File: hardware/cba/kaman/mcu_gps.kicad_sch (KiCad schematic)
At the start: 12 parts, among them Q1 MMDT5551, SW1 SW_Push, SW2 SW_Push, U1 ESP32-C6-WROOM-1-N8

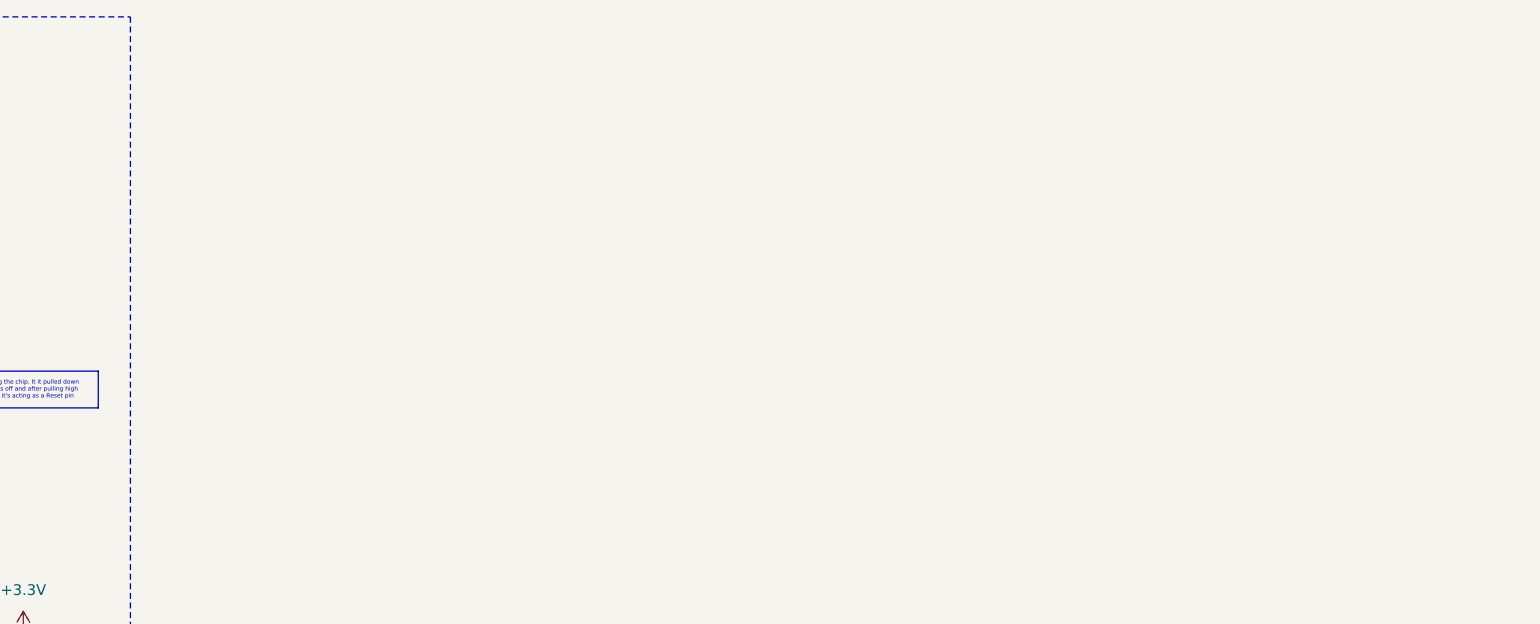
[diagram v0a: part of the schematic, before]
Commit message: hw(schmatic): add L80 GPS Module
L80 and the circuit such as the decoupling caps,reset and PPS pin, and
most importantly the backup battery (although the footprint has to be
checked)
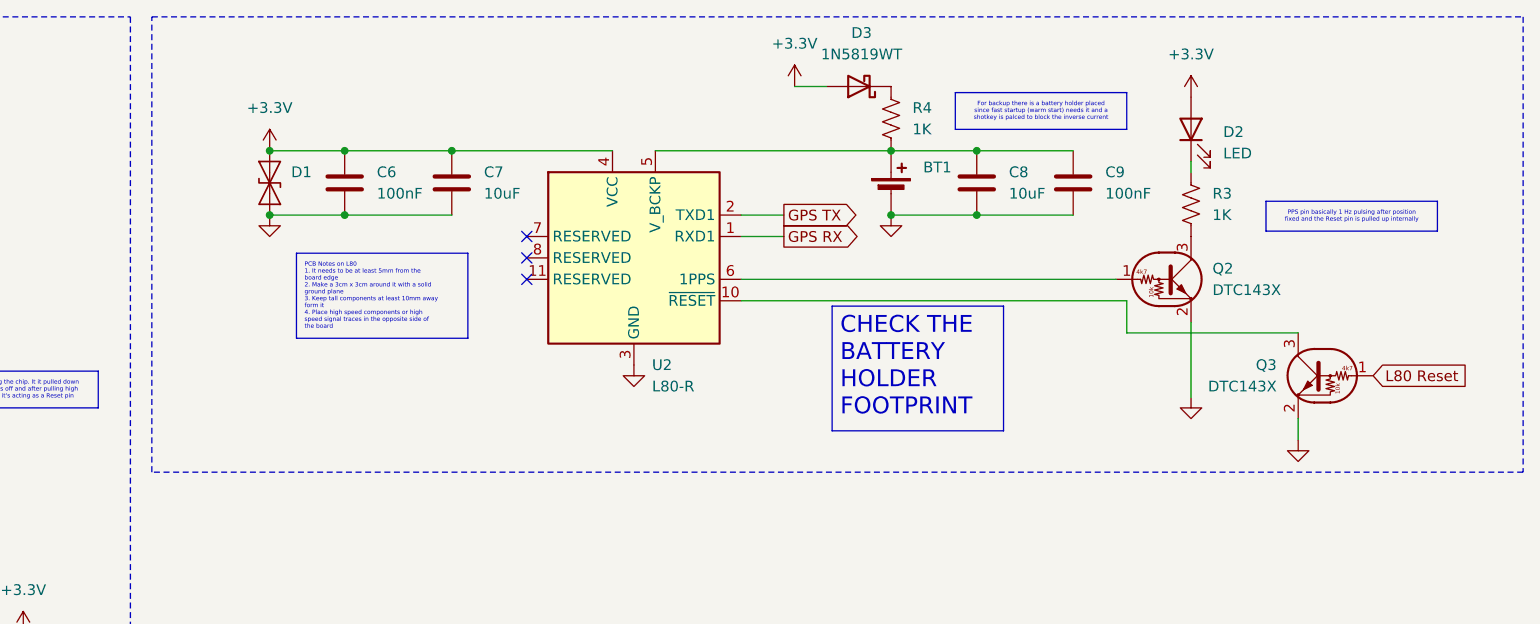
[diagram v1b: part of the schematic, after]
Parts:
- added BT1: Battery_Cell, Battery:BatteryHolder_Keystone_1060_1x2032, symbol Device:Battery_Cell
- added C6, C9: 100nF, Capacitor_SMD:C_0603_1608Metric_Pad1.08x0.95mm_HandSolder, symbol Device:C
- added C7, C8: 10uF, Capacitor_SMD:C_0805_2012Metric_Pad1.18x1.45mm_HandSolder, symbol Device:C
- added D1: SD03C-MMD, Diode_SMD:D_SOD-323_HandSoldering, symbol Diode:SD05C-01F
- added D2: LED, LED_SMD:LED_0603_1608Metric_Pad1.05x0.95mm_HandSolder, symbol Device:LED
- added D3: 1N5819WT, Diode_SMD:D_SOD-523, symbol Diode:1N5819WS
- added Q2, Q3: DTC143X, symbol Transistor_BJT:DTC143X
- added R3, R4: 1K, Resistor_SMD:R_0603_1608Metric_Pad0.98x0.95mm_HandSolder, symbol Device:R_US
- added U2: L80-R, RF_GPS:Quectel_L80-R, symbol RF_GPS:L80-R
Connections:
- net +3.3V: now also C6.1, C7.1, D1.2 (A2), D2.2 (A), D3.2 (A), U2.4 (VCC)
- net GND: now also BT1.2 (-), C6.2, C7.2, C8.2, C9.2, D1.1 (A1), Q2.2 (E), Q3.2 (E), U2.12 (GND), U2.3 (GND)
- new net: D3.1 (K), R4.1
- new net: BT1.1 (+), C8.1, C9.1, R4.2, U2.5 (V_BCKP)
- new net: Q3.3 (C), U2.10 (~{RESET})
- new net: Q2.1 (B), U2.6 (1PPS)
- new net: Q2.3 (C), R3.2
- new net: D2.1 (K), R3.1
- new net GPS RX: U2.1 (RXD1)
- new net GPS TX: U2.2 (TXD1)
- new net L80 Reset: Q3.1 (B)
- no-connect marks 0 -> 3

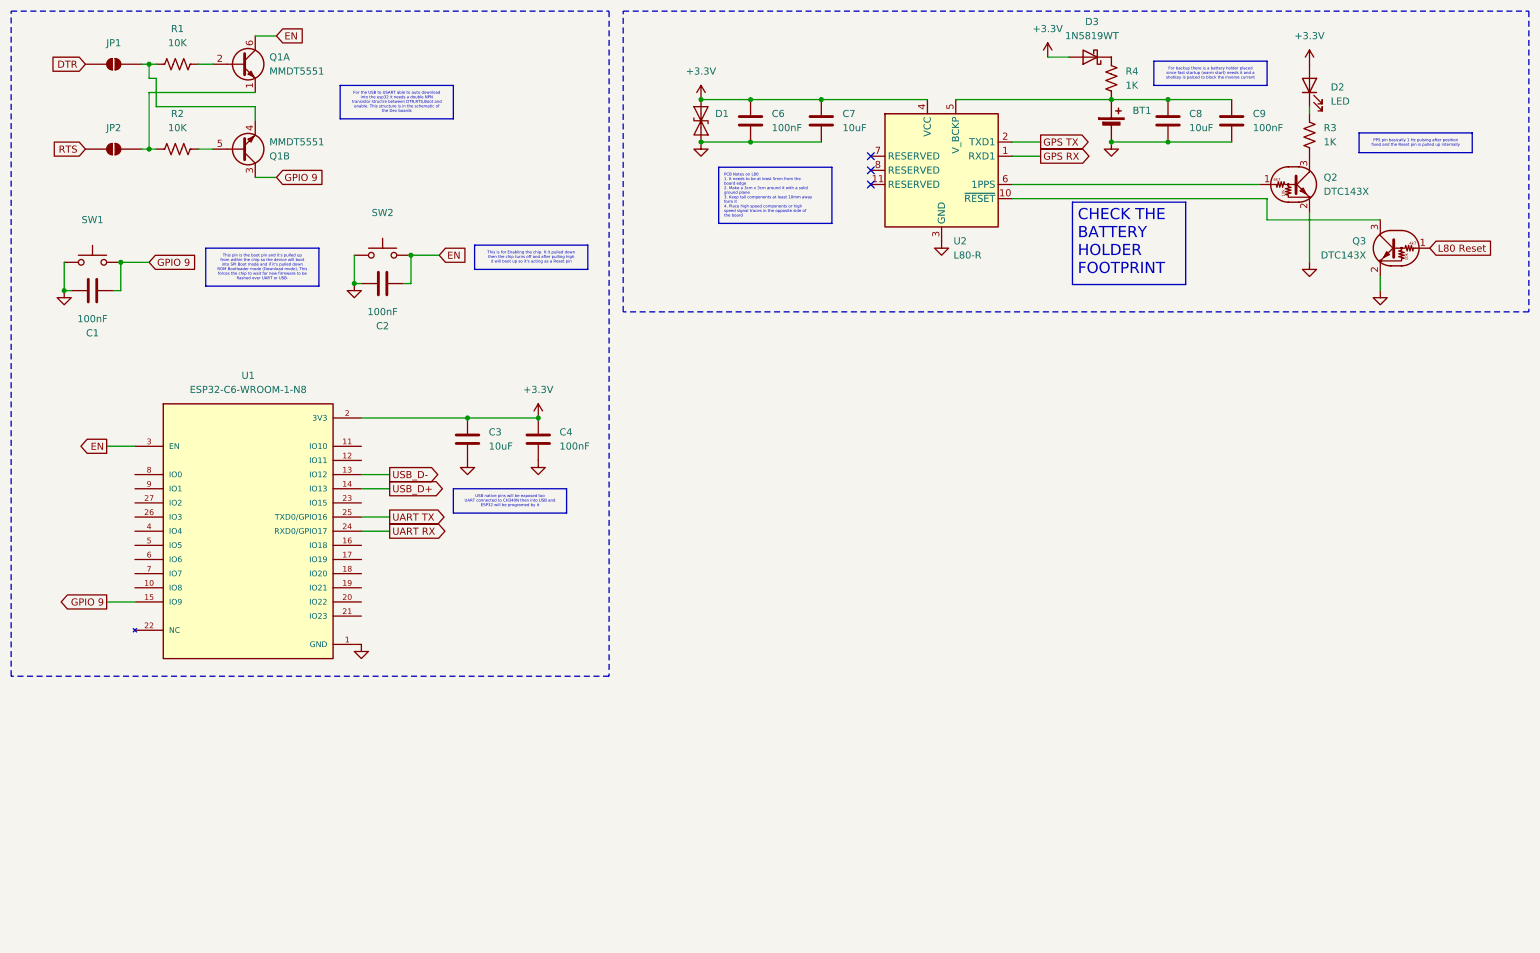
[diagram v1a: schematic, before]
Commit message: hw(schematic): add NEO-MXN GPS module
Add U blox NEO GPS module which has the same footprint even with change
of generations and the EEPROM IC,antenna and the battery holder
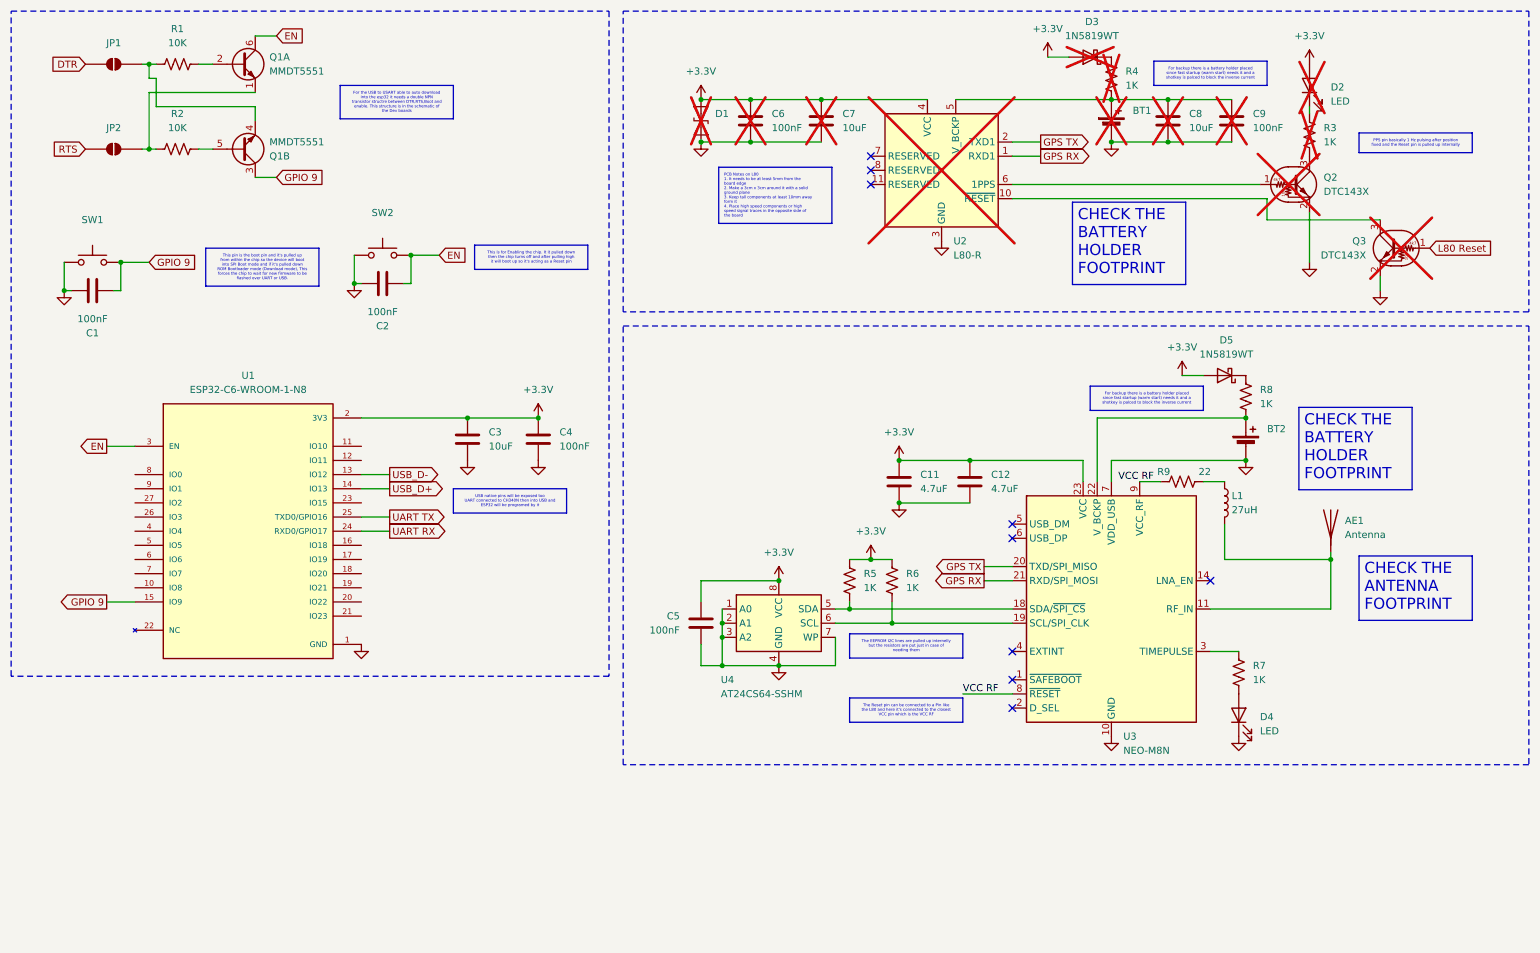
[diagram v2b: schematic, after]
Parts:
- added AE1: Antenna, Connector_Coaxial:U.FL_Molex_MCRF_73412-0110_Vertical, symbol Device:Antenna
- added BT2: Battery_Cell, Battery:BatteryHolder_Keystone_1060_1x2032, symbol Device:Battery_Cell
- added C11, C12: 4.7uF, Capacitor_SMD:C_0805_2012Metric_Pad1.18x1.45mm_HandSolder, symbol Device:C
- added C5: 100nF, Capacitor_SMD:C_0603_1608Metric_Pad1.08x0.95mm_HandSolder, symbol Device:C
- added D4: LED, LED_SMD:LED_0603_1608Metric_Pad1.05x0.95mm_HandSolder, symbol Device:LED
- added D5: 1N5819WT, Diode_SMD:D_SOD-523, symbol Diode:1N5819WS
- added L1: 27uH, Inductor_SMD:L_1812_4532Metric_Pad1.30x3.40mm_HandSolder, symbol Device:L
- added R5, R6, R7, R8: 1K, Resistor_SMD:R_0603_1608Metric_Pad0.98x0.95mm_HandSolder, symbol Device:R_US
- added R9: 22, Resistor_SMD:R_0603_1608Metric_Pad0.98x0.95mm_HandSolder, symbol Device:R_US
- added U3: NEO-M8N, RF_GPS:ublox_NEO, symbol RF_GPS:NEO-M8N
- added U4: AT24CS64-SSHM, Package_SO:SOIC-8_3.9x4.9mm_P1.27mm, symbol Memory_EEPROM:AT24CS64-SSHM
- BT1, C6, C7, C8, C9, D1, D2, D3, Q2, Q3, R3, R4, U2: now not fitted
- C3: footprint Capacitor_SMD:C_1206_3216Metric -> Capacitor_SMD:C_0805_2012Metric_Pad1.18x1.45mm_HandSolder
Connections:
- net +3.3V: now also C11.1, C12.1, C5.1, D5.2 (A), R5.1, R6.1, U3.23 (VCC), U4.8 (VCC)
- net GND: now also BT2.2 (-), C11.2, C12.2, C5.2, D4.1 (K), U3.10 (GND), U3.12 (GND), U3.13 (GND), U3.24 (GND), U3.7 (VDD_USB), U4.1 (A0), U4.2 (A1), U4.3 (A2), U4.4 (GND), U4.7 (WP)
- net GPS RX: now also U3.21 (RXD/SPI_MOSI)
- net GPS TX: now also U3.20 (TXD/SPI_MISO)
- new net: D4.2 (A), R7.2
- new net: D5.1 (K), R8.1
- new net: BT2.1 (+), R8.2, U3.22 (V_BCKP)
- new net: L1.1, R9.2
- new net: AE1.1 (A), L1.2, U3.11 (RF_IN)
- new net: R7.1, U3.3 (TIMEPULSE)
- new net: R6.2, U3.19 (SCL/SPI_CLK), U4.6 (SCL)
- new net: R5.2, U3.18 (SDA/~{SPI_CS}), U4.5 (SDA)
- new net VCC RF: R9.1, U3.8 (~{RESET}), U3.9 (VCC_RF)
- no-connect marks 3 -> 9

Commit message: hw(schematic): add oled and gps module connector
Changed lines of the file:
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@@
 	)
 	(global_label "GPIO 9"
-		(shape output)
+		(shape passive)
 		(at 29.21 118.11 180)
 		(fields_autoplaced yes)
@@
 		)
 		(property "Intersheetrefs" "${INTERSHEET_REFS}"
-			(at 19.5724 118.11 0)
+			(at 20.6837 118.11 0)
 			(hide yes)
 			(show_name no)
@@
 	)
 	(global_label "GPS RX"
-		(shape output)
+		(shape input)
 		(at 196.85 38.1 0)
 		(fields_autoplaced yes)
@@
 	)
 	(global_label "EN"
-		(shape output)
+		(shape passive)
 		(at 29.21 90.17 180)
 		(fields_autoplaced yes)
@@
 		)
 		(property "Intersheetrefs" "${INTERSHEET_REFS}"
-			(at 23.7453 90.17 0)
+			(at 24.8566 90.17 0)
 			(hide yes)
 			(show_name no)
@@
 	)
 	(global_label "USB_D+"
-		(shape output)
+		(shape bidirectional)
 		(at 80.01 97.79 0)
 		(fields_autoplaced yes)
@@
 		)
 		(property "Intersheetrefs" "${INTERSHEET_REFS}"
-			(at 90.6152 97.79 0)
+			(at 91.7265 97.79 0)
 			(hide yes)
 			(show_name no)
@@
 	)
 	(global_label "UART RX"
-		(shape output)
+		(shape input)
 		(at 80.01 105.41 0)
 		(fields_autoplaced yes)
@@
 	)
 	(global_label "GPS RX"
-		(shape output)
+		(shape input)
 		(at 186.69 114.3 180)
 		(fields_autoplaced yes)
@@
 	)
 	(global_label "USB_D-"
-		(shape output)
+		(shape bidirectional)
 		(at 80.01 95.25 0)
 		(fields_autoplaced yes)
@@
 		)
 		(property "Intersheetrefs" "${INTERSHEET_REFS}"
-			(at 90.6152 95.25 0)
+			(at 91.7265 95.25 0)
 			(hide yes)
 			(show_name no)
@@
 		(exclude_from_sim no)
 		(in_bom yes)
-		(on_board yes)
+		(on_board no)
 		(in_pos_files yes)
 		(dnp yes)
@@
 		(exclude_from_sim no)
 		(in_bom yes)
-		(on_board yes)
+		(on_board no)
 		(in_pos_files yes)
 		(dnp yes)
@@
 		(exclude_from_sim no)
 		(in_bom yes)
-		(on_board yes)
+		(on_board no)
 		(in_pos_files yes)
 		(dnp yes)
@@
 		(exclude_from_sim no)
 		(in_bom yes)
-		(on_board yes)
+		(on_board no)
 		(in_pos_files yes)
 		(dnp yes)
@@
 		(exclude_from_sim no)
 		(in_bom yes)
-		(on_board yes)
+		(on_board no)
 		(in_pos_files yes)
 		(dnp yes)
@@
 		(exclude_from_sim no)
 		(in_bom yes)
-		(on_board yes)
+		(on_board no)
 		(in_pos_files yes)
 		(dnp yes)
@@
 		(exclude_from_sim no)
 		(in_bom yes)
-		(on_board yes)
+		(on_board no)
 		(in_pos_files yes)
 		(dnp yes)
@@
 		(exclude_from_sim no)
 		(in_bom yes)
-		(on_board yes)
+		(on_board no)
 		(in_pos_files yes)
 		(dnp yes)
@@
 		(exclude_from_sim no)
 		(in_bom yes)
-		(on_board yes)
+		(on_board no)
 		(in_pos_files yes)
 		(dnp yes)
@@
 		(exclude_from_sim no)
 		(in_bom yes)
-		(on_board yes)
+		(on_board no)
 		(in_pos_files yes)
 		(dnp yes)
@@
 		(exclude_from_sim no)
 		(in_bom yes)
-		(on_board yes)
+		(on_board no)
 		(in_pos_files yes)
 		(dnp yes)
@@
 		(exclude_from_sim no)
 		(in_bom yes)
-		(on_board yes)
+		(on_board no)
 		(in_pos_files yes)
 		(dnp yes)
@@
 		(exclude_from_sim no)
 		(in_bom yes)
-		(on_board yes)
+		(on_board no)
 		(in_pos_files yes)
 		(dnp yes)

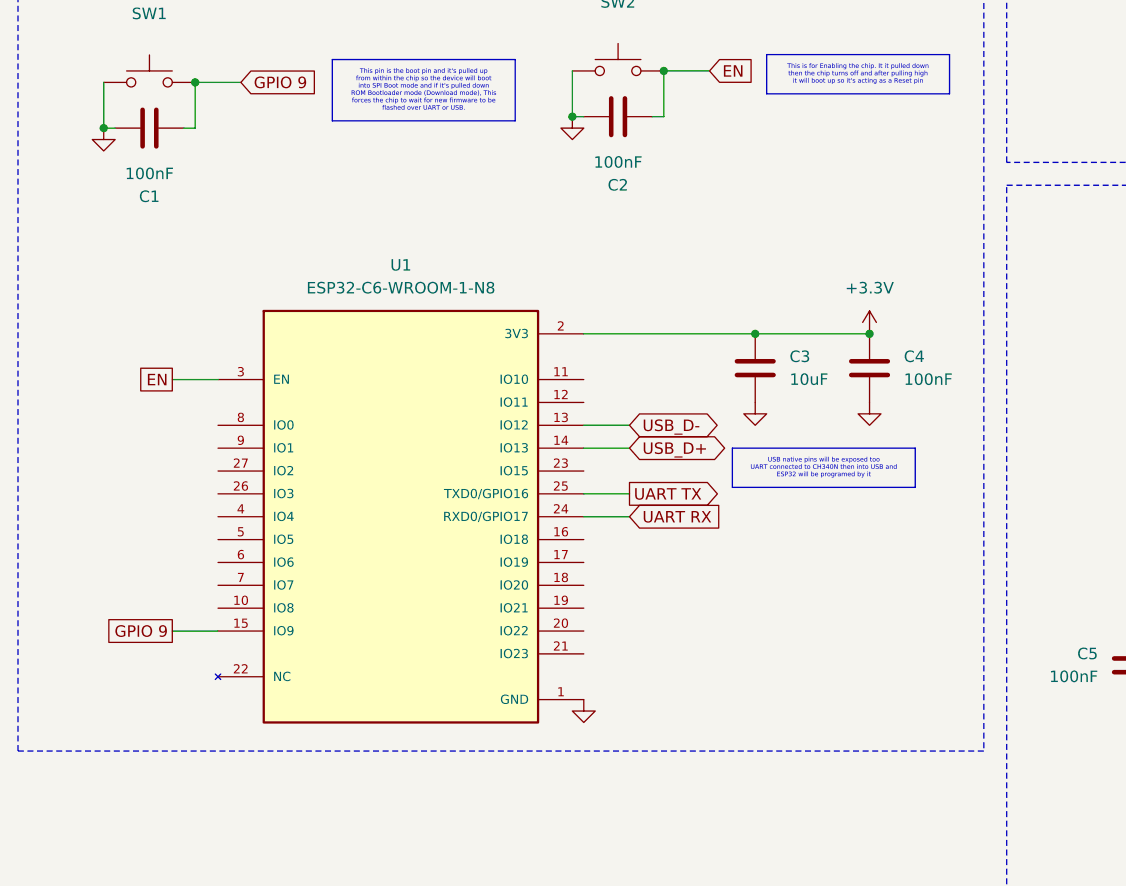
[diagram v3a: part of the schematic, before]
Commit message: hw(schematic): change main mcu version
Change ESP32 C6 WROOM to the mini version due to size constraints on pcb
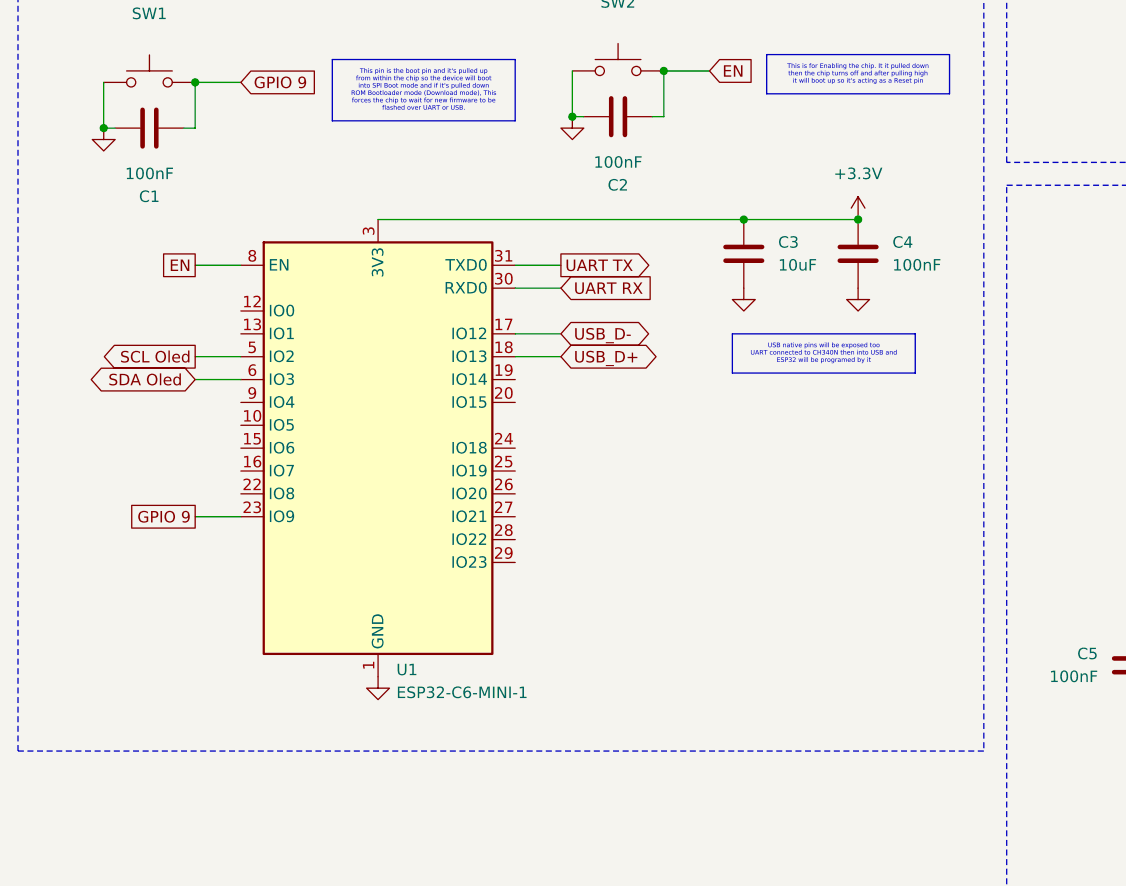
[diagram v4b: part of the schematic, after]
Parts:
- removed U1: ESP32-C6-WROOM-1-N8, Library:ESP32-C6-WROOM-1-N8, symbol ESP32-C6-WROOM-1-N8:ESP32-C6-WROOM-1-N8
- added U1: ESP32-C6-MINI-1, RF_Module:ESP32-C6-MINI-1, symbol RF_Module:ESP32-C6-MINI-1
- AE1: footprint Connector_Coaxial:U.FL_Molex_MCRF_73412-0110_Vertical -> Connector_Coaxial:U.FL_Hirose_U.FL-R-SMT-1_Vertical
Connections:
- net +3.3V: now also U1.3 (3V3)
- net EN: now also U1.8 (EN)
- net GND: now also U1.1 (GND), U1.11 (GND), U1.14 (GND), U1.2 (GND), U1.36 (GND), U1.37 (GND), U1.38 (GND), U1.39 (GND), U1.40 (GND), U1.41 (GND), U1.42 (GND), U1.43 (GND), U1.44 (GND), U1.45 (GND), U1.46 (GND), U1.47 (GND), U1.48 (GND), U1.49 (GND), U1.50 (GND), U1.51 (GND), U1.52 (GND), U1.53 (GND)
- net GPIO 9: now also U1.23 (IO9)
- net UART RX: now also U1.30 (RXD0)
- net UART TX: now also U1.31 (TXD0)
- net USB_D+: now also U1.18 (IO13)
- net USB_D-: now also U1.17 (IO12)
- new net SCL Oled: U1.5 (IO2)
- new net SDA Oled: U1.6 (IO3)
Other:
- moved on the sheet: C3, C4

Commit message: hw(pcb): add missing 3d models for parts
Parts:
- D1: footprint Diode_SMD:D_SOD-323_HandSoldering -> Diode_SMD:D_SOD-323
- D3, D5: footprint Diode_SMD:D_SOD-523 -> Diode_SMD:D_SOD-323
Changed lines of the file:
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@@
 			)
 		)
-		(property "Footprint" "Diode_SMD:D_SOD-523"
+		(property "Footprint" "Diode_SMD:D_SOD-323"
 			(at 205.74 15.875 0)
 			(hide yes)
@@
 			)
 		)
-		(property "Footprint" "Diode_SMD:D_SOD-523"
+		(property "Footprint" "Diode_SMD:D_SOD-323"
 			(at 229.87 73.025 0)
 			(hide yes)
@@
 			)
 		)
-		(property "Footprint" "Diode_SMD:D_SOD-323_HandSoldering"
+		(property "Footprint" "Diode_SMD:D_SOD-323"
 			(at 140.97 31.75 0)
 			(hide yes)
